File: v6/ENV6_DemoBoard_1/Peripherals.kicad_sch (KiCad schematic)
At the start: 21 parts, among them J301 Micro_SD_Card, J302 Conn_01x03_Pin, J303 Conn_02x02_Odd_Even, J304 Conn_02x02_Odd_Even, J305 Conn_02x02_Odd_Even, J306 Conn_02x02_Odd_Even, U301 PAC1954x-x4MX

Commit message: ENV6 (test): Changes after first review
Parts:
- removed J302: Conn_01x03_Pin, Connector_PinSocket_2.54mm:PinSocket_1x03_P2.54mm_Vertical, symbol Connector:Conn_01x03_Pin
- removed R303, R304: 10kR, Resistor_SMD:R_0603_1608Metric, symbol Device:R
- added J2: SHIELD_ARDUINO-UNO, connectors:arduino_uno_full, symbol connectors:Arduino Uno-Shield (Full)
- C301: value 100nF -> 100n
- C302: value 10uF -> 10µ
- C303: value 4.7uF -> 4µ7
- C304: value 0.1uF -> 100n
- R302: value 10kR -> 10k
- R305, R306: value 0R -> 0R1
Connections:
- net PAC_PWRDN: no longer names the net of R302.2, U301.16 (~{PWRDN})
- net PAC_SLOW: no longer names the net of R306.1, U301.1 (SLOW)
- new net: J2.G0 (GND), J2.G1 (GND), J2.G2 (GND)
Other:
- note added: "Add it to the MCU"
- note added: "Add these pins to the FPGA board"
- note added: "Sensing PAC #1 (MCU board) - 3V3 wireless - 3V3 only MCU - 3V3 MCU flash - 3v3 MCU peripherie (outside via connector)"
- note added: "Sensing PAC #2 (FPGA board) - FPGA core (1V8) - FPGA core (1V1) - FPGA peripherie (3V3) - FPGA IO-banks + flash (3V3)"
- note added: "Sensing PAC #3 (Power directly) - Input - Line output 1 - Line output 2 - Line output 3 - Line output 4 (?)"
- moved on the sheet: R302, R306

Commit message: new PSU and updates
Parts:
- removed J303, J304, J305, J306: Conn_02x02_Odd_Even, Connector_PinHeader_2.54mm:PinHeader_2x02_P2.54mm_Vertical, symbol Connector_Generic:Conn_02x02_Odd_Even
- added C14: 4µ7, Capacitor_SMD:C_0603_1608Metric, symbol Device:C
- added C15: 100n, Capacitor_SMD:C_0603_1608Metric, symbol Device:C
- added J401: Conn_02x12_Odd_Even, Connector_PinSocket_2.54mm:PinSocket_2x12_P2.54mm_Vertical, symbol Connector_Generic:Conn_02x12_Odd_Even
- added R5, R6: 0R1, Resistor_SMD:R_0603_1608Metric, symbol Device:R
- added R7: 10k, Resistor_SMD:R_0603_1608Metric, symbol Device:R
- added RS5, RS6, RS7, RS8: 0.82R, Resistor_SMD:R_0603_1608Metric, symbol Device:R
- added U2: PAC1954x-x4MX, Package_DFN_QFN:VQFN-16-1EP_3x3mm_P0.5mm_EP1.1x1.1mm, symbol Sensor_Energy:PAC1954x-x4MX
- J2: now not fitted; now left out of the parts list
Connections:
- net GND: now also C14.2, C15.2, R5.2, R6.2, U2.17 (EP), U2.3 (GND)
- net GP0/I2C0_SDA: now also U2.5 (SDA)
- net GP1/I2C0_SCL: now also U2.4 (SCL)
- net PSU_OUT1: now also RS5.2, U2.11 (SENSE1+); no longer RS1.2, U301.11 (SENSE1+)
- net PSU_OUT2: now also RS6.2, U2.13 (SENSE2+); no longer RS2.2, U301.13 (SENSE2+)
- net PSU_OUT3: now also RS7.2, U2.8 (SENSE3+); no longer RS3.2, U301.8 (SENSE3+)
- net PSU_OUT4: now also RS8.2, U2.10 (SENSE4+); no longer RS4.2, U301.10 (SENSE4+)
- net V1: now also J401.1 (Pin_1), J401.2 (Pin_2), J401.3 (Pin_3), J401.4 (Pin_4), RS5.1, U2.12 (SENSE1-); no longer RS1.1, U301.12 (SENSE1-)
- net V2: now also J401.10 (Pin_10), J401.7 (Pin_7), J401.8 (Pin_8), J401.9 (Pin_9), RS6.1, U2.14 (SENSE2-); no longer RS2.1, U301.14 (SENSE2-)
- net V3: now also J401.13 (Pin_13), J401.14 (Pin_14), J401.15 (Pin_15), J401.16 (Pin_16), RS7.1, U2.7 (SENSE3-); no longer RS3.1, U301.7 (SENSE3-)
- net V4: now also J401.19 (Pin_19), J401.20 (Pin_20), J401.21 (Pin_21), J401.22 (Pin_22), RS8.1, U2.9 (SENSE4-); no longer RS4.1, U301.9 (SENSE4-)
- net VCC_MCU: now also C14.1, C15.1, R7.1, U2.2 (V_{DD}); no longer C301.2, C302.2, J301.4 (VDD)
- net PAC_GPIO renamed PAC1_GPIO
- new net: R6.1, U2.1 (SLOW)
- new net: R7.2, U2.16 (~{PWRDN})
- new net: R5.1, U2.6 (ADDRSEL)
- new net 3V3_MCU: RS1.2, RS2.2, RS3.2, RS4.2, U301.10 (SENSE4+), U301.11 (SENSE1+), U301.13 (SENSE2+), U301.8 (SENSE3+)
- new net 3V3_MCU_FLASH: RS3.1, U301.7 (SENSE3-)
- new net 3V3_MCU_Per: C301.2, C302.2, J301.4 (VDD), RS4.1, U301.9 (SENSE4-)
- new net 3V3_MCU_only: RS1.1, U301.12 (SENSE1-)
- new net 3V3_Pi_Radio: RS2.1, U301.14 (SENSE2-)
- new net PAC2_GPIO: U2.15 (GPIO)
- no-connect marks 2 -> 10
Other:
- note added: "PAC1954 (1)"
- note added: "PAC1954 (2)"
- note added: "Sensing PAC #2 (Power directly) - Input - Line output 1 - Line output 2 - Line output 3 - Line output 4 (?)"
- note added: "Sensing PAC #3(FPGA board) - FPGA core (1V8) - FPGA core (1V1) - FPGA peripherie (3V3) - FPGA IO-banks + flash (3V3)"
- note removed: "PAC1954"
- note removed: "Sensing PAC #2 (FPGA board) - FPGA core (1V8) - FPGA core (1V1) - FPGA peripherie (3V3) - FPGA IO-banks + flash (3V3)"
- note removed: "Sensing PAC #3 (Power directly) - Input - Line output 1 - Line output 2 - Line output 3 - Line output 4 (?)"
- moved on the sheet: C301, C302, C303, C304, J301, R301, R302, R305, R306, RS1, RS2, RS3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

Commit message: Changes after second rev of ENV6 test
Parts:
- removed C14, C303: 4µ7, Capacitor_SMD:C_0603_1608Metric, symbol Device:C
- removed C15, C304: 100n, Capacitor_SMD:C_0603_1608Metric, symbol Device:C
- removed J2: SHIELD_ARDUINO-UNO, connectors:arduino_uno_full, symbol connectors:Arduino Uno-Shield (Full)
- removed J401: Conn_02x12_Odd_Even, Connector_PinSocket_2.54mm:PinSocket_2x12_P2.54mm_Vertical, symbol Connector_Generic:Conn_02x12_Odd_Even
- removed R301: 10kR, Resistor_SMD:R_0603_1608Metric, symbol Device:R
- removed R302, R7: 10k, Resistor_SMD:R_0603_1608Metric, symbol Device:R
- removed R305, R306, R5, R6: 0R1, Resistor_SMD:R_0603_1608Metric, symbol Device:R
- removed RS1, RS2, RS3, RS4, RS5, RS6, RS7, RS8: 0.82R, Resistor_SMD:R_0603_1608Metric, symbol Device:R
- removed U2, U301: PAC1954x-x4MX, Package_DFN_QFN:VQFN-16-1EP_3x3mm_P0.5mm_EP1.1x1.1mm, symbol Sensor_Energy:PAC1954x-x4MX
- added C26, C45, C49: 10u, Capacitor_SMD:C_0402_1005Metric, symbol passive:C0402
- added C27, C46, C50: 100n, Capacitor_SMD:C_0402_1005Metric, symbol passive:C0402
- added R14, R16, R21, R23, R24, R25, R29, R31, R32, R33, R36: 0R82, Resistor_SMD:R_0402_1005Metric, symbol passive:R0402
- added R15, R22, R28, R30: 10k, Resistor_SMD:R_0402_1005Metric, symbol passive:R0402
- added R17: 100k, Resistor_SMD:R_0402_1005Metric, symbol passive:R0402
- added R18, R27, R34, R35: 750R, Resistor_SMD:R_0402_1005Metric, symbol passive:R0402
- added R26: 0R1, Resistor_SMD:R_0402_1005Metric, symbol passive:R0402
- added U5, U7, U8: PAC1954x-x4MX, Package_DFN_QFN:VQFN-16-1EP_3x3mm_P0.5mm_EP1.1x1.1mm, symbol sensors:PAC1954x-x4MX
- C48: renamed from C302; value 10µ -> 10u
- renumbered C301 to C47, J301 to J2
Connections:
- net GND: now also C26.1, C27.1, C45.1, C46.1, C49.1, C50.1, R17.2, R18.2, R26.2, R27.2, R34.2, R35.2, U5.17 (EP), U5.3 (GND), U7.17 (EP), U7.3 (GND), U8.17 (EP), U8.3 (GND)
- net GP0/I2C0_SDA: now also U5.5 (SDA), U7.5 (SDA), U8.5 (SDA)
- net GP1/I2C0_SCL: now also U5.4 (SCL), U7.4 (SCL), U8.4 (SCL)
- net GP5/SPI0_CS: now also R28.1
- net PSU_OUT1: now also R29.2, U8.11 (SENSE1+)
- net PSU_OUT2: now also R31.2, U8.13 (SENSE2+)
- net PSU_OUT3: now also R32.2, U8.8 (SENSE3+)
- net PSU_OUT4: now also R33.2, U8.10 (SENSE4+)
- net V1: now also R29.1, U8.12 (SENSE1-)
- net V2: now also R31.1, U8.14 (SENSE2-)
- net V3: now also R32.1, U8.7 (SENSE3-)
- net V4: now also R33.1, U8.9 (SENSE4-)
- net 3V3_MCU_Per renamed VDDD_PERI
- net VDDD_PERI: now also C26.2, C27.2, C45.2, C46.2, C49.2, C50.2, R15.1, R22.1, R25.1, R28.2, R30.1, U5.2 (V_{DD}), U7.2 (V_{DD}), U7.9 (SENSE4-), U8.2 (V_{DD})
- new net: R18.1, U5.1 (SLOW)
- new net: R14.1, U5.12 (SENSE1-)
- new net: R15.2, U5.16 (~{PWRDN})
- new net: R17.1, U5.6 (ADDRSEL)
- new net: R30.2, U8.16 (~{PWRDN})
- new net: R34.1, U8.6 (ADDRSEL)
- new net: R22.2, U7.16 (~{PWRDN})
- new net: R26.1, U7.6 (ADDRSEL)
- new net: R35.1, U8.1 (SLOW)
- new net: R27.1, U7.1 (SLOW)
- new net VDDD_FLASH: R24.1, U7.7 (SENSE3-)
- new net VDDD_MCU: R21.1, U7.12 (SENSE1-)
- new net VDDD_RADIO: R23.1, U7.14 (SENSE2-)
- new net VDIG_IN: R16.1, U5.14 (SENSE2-)
- new net VDIG_OUT: R21.2, R23.2, R24.2, R25.2, U7.10 (SENSE4+), U7.11 (SENSE1+), U7.13 (SENSE2+), U7.8 (SENSE3+)
- new net VPERI_IN: R36.1, U5.7 (SENSE3-)
- new net VSYS_IN: R14.2, R16.2, R36.2, U5.11 (SENSE1+), U5.13 (SENSE2+), U5.8 (SENSE3+)
- no-connect marks 10 -> 7
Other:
- note added: "1, Peripherals"
- note added: "I2C Addr: 0x10"
- note added: "I2C Addr: 0x12"
- note added: "I2C Addr: 0x1C"
- note added: "PAC1954 (3)"
- note added: "Sensing PAC #1 - 3V3 wireless - 3V3 only MCU - 3V3 MCU flash - 3v3 peri"
- note added: "Sensing PAC #2 - Line output 1 - Line output 2 - Line output 3 - Line output 4"
- note added: "Sensing PAC #3(FPGA board) - FPGA core (1V8) - FPGA core (1V1) - FPGA peripherie (3V3) - FPGA IO-banks + flash (3V3) Acutally it is doubled, maybe remove it?"
- note added: "Sensing PAC #4 - V_SYS Input - V_DIG - V_APP - ???"
- note added: "find a link to buy sense resistors (0.1% accuracy, high power budget)"
- note removed: "3, Peripherals"
- note removed: "Add it to the MCU"
- note removed: "Add these pins to the FPGA board"
- note removed: "Sensing PAC #1 (MCU board) - 3V3 wireless - 3V3 only MCU - 3V3 MCU flash - 3v3 MCU peripherie (outside via connector)"
- note removed: "Sensing PAC #2 (Power directly) - Input - Line output 1 - Line output 2 - Line output 3 - Line output 4 (?)"
- note removed: "Sensing PAC #3(FPGA board) - FPGA core (1V8) - FPGA core (1V1) - FPGA peripherie (3V3) - FPGA IO-banks + flash (3V3)"
- note removed: "Voltage Outputs"
- moved on the sheet: C47, C48, J2

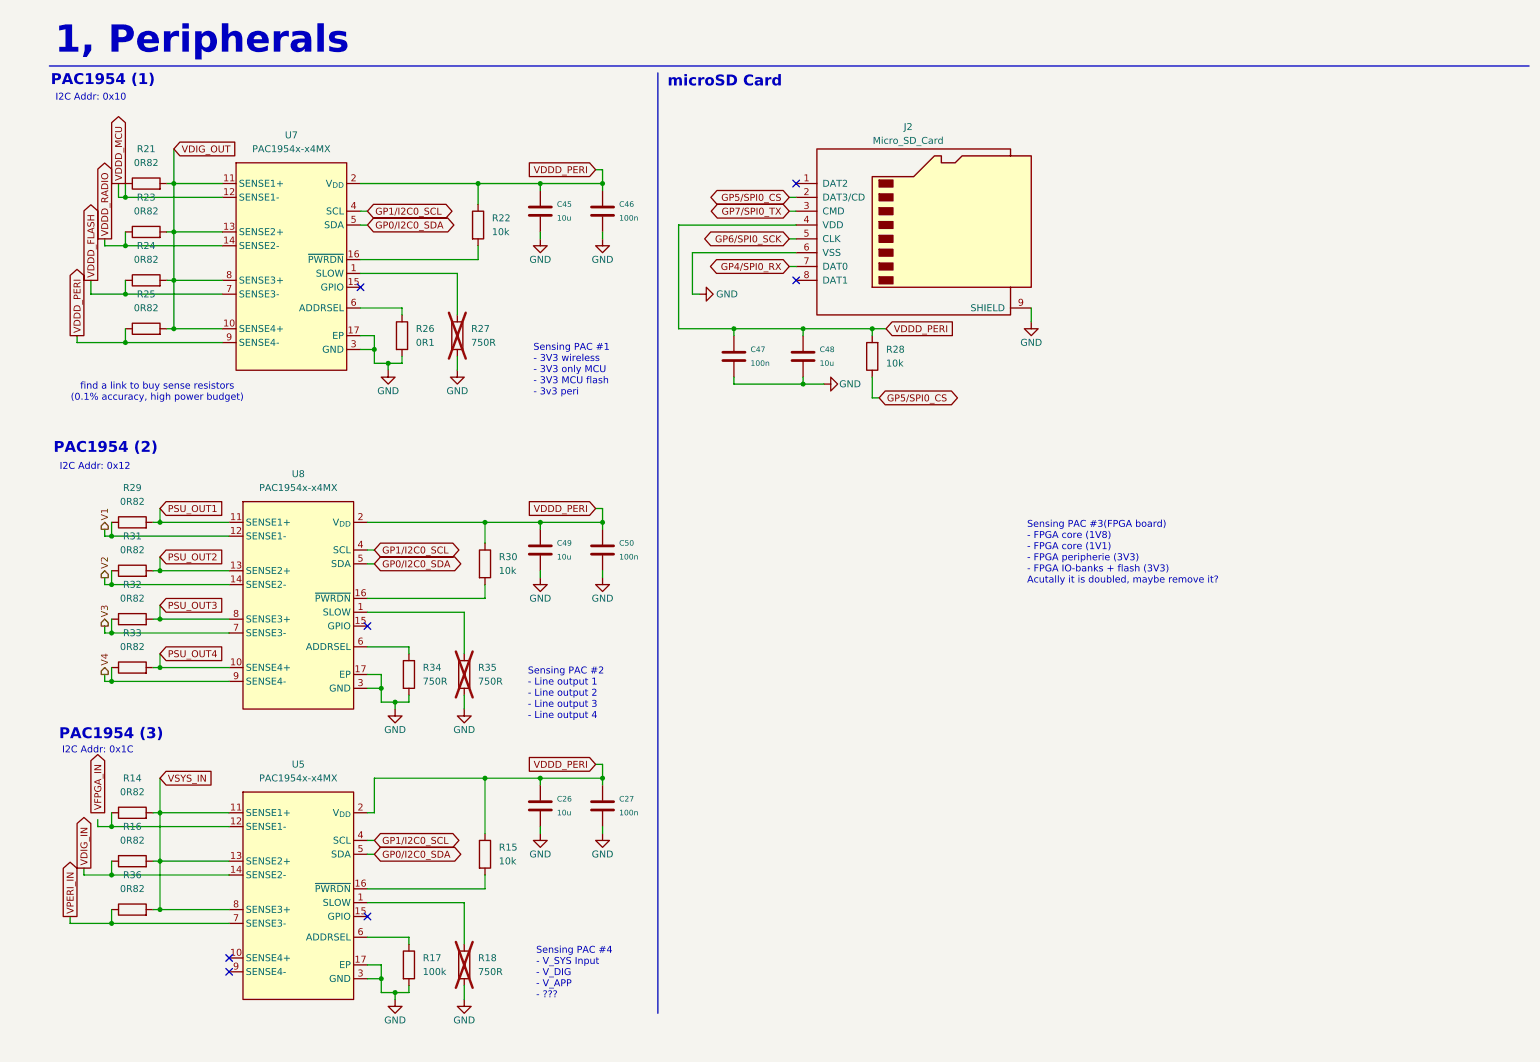
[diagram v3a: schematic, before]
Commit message: update Demoboard and add GateMateA11 board
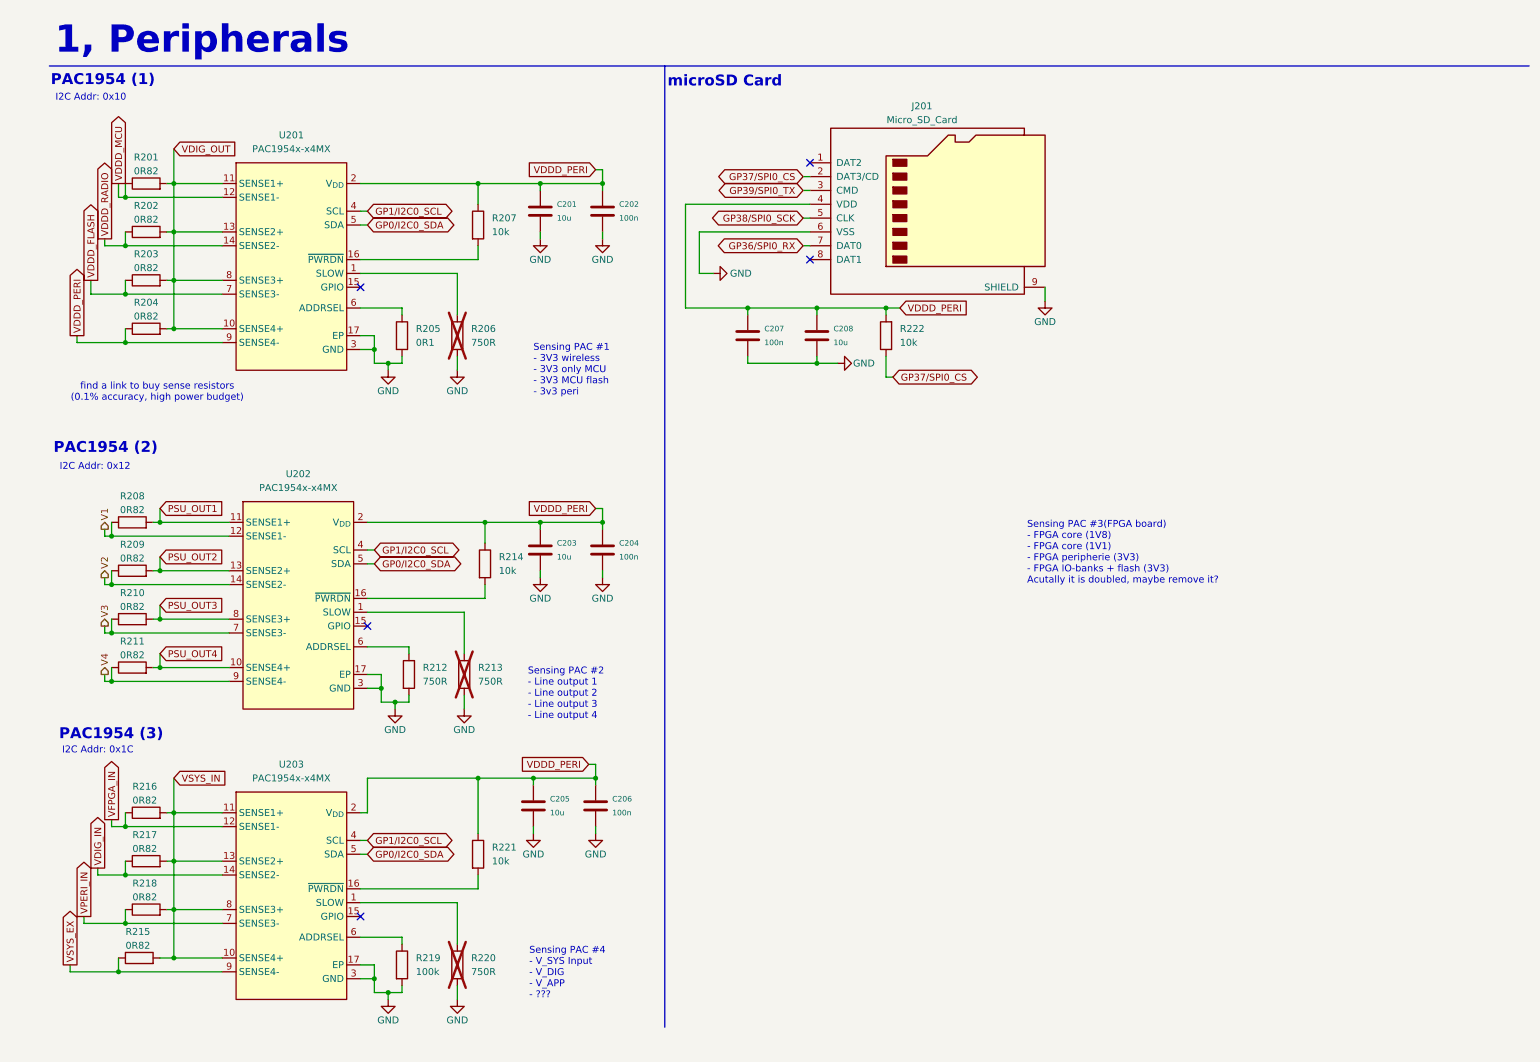
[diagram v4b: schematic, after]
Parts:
- added R215: 0R82, Resistor_SMD:R_0603_1608Metric, symbol passive:R0402
- R201: renamed from R21; footprint Resistor_SMD:R_0402_1005Metric -> Resistor_SMD:R_0603_1608Metric
- R202: renamed from R23; footprint Resistor_SMD:R_0402_1005Metric -> Resistor_SMD:R_0603_1608Metric
- R203: renamed from R24; footprint Resistor_SMD:R_0402_1005Metric -> Resistor_SMD:R_0603_1608Metric
- R204: renamed from R25; footprint Resistor_SMD:R_0402_1005Metric -> Resistor_SMD:R_0603_1608Metric
- R208: renamed from R29; footprint Resistor_SMD:R_0402_1005Metric -> Resistor_SMD:R_0603_1608Metric
- R209: renamed from R31; footprint Resistor_SMD:R_0402_1005Metric -> Resistor_SMD:R_0603_1608Metric
- R210: renamed from R32; footprint Resistor_SMD:R_0402_1005Metric -> Resistor_SMD:R_0603_1608Metric
- R211: renamed from R33; footprint Resistor_SMD:R_0402_1005Metric -> Resistor_SMD:R_0603_1608Metric
- R216: renamed from R14; footprint Resistor_SMD:R_0402_1005Metric -> Resistor_SMD:R_0603_1608Metric
- R217: renamed from R16; footprint Resistor_SMD:R_0402_1005Metric -> Resistor_SMD:R_0603_1608Metric
- R218: renamed from R36; footprint Resistor_SMD:R_0402_1005Metric -> Resistor_SMD:R_0603_1608Metric
- renumbered C45 to C201, C46 to C202, C49 to C203, C50 to C204, C26 to C205, C27 to C206, C47 to C207, C48 to C208, J2 to J201, R26 to R205, R27 to R206, R22 to R207, R34 to R212, R35 to R213, R30 to R214, R17 to R219, R18 to R220, R15 to R221, R28 to R222, U7 to U201, U8 to U202, U5 to U203
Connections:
- net VFPGA_IN: now also R216.1, U203.12 (SENSE1-)
- net VSYS_IN: now also U203.10 (SENSE4+), R215.2
- net VSYS_EX: now reaches U203.9 (SENSE4-)
- net VSYS_EX: now also R215.1
- net GP4/SPI0_RX renamed GP36/SPI0_RX
- net GP5/SPI0_CS renamed GP37/SPI0_CS
- net GP6/SPI0_SCK renamed GP38/SPI0_SCK
- net GP7/SPI0_TX renamed GP39/SPI0_TX
- no-connect marks 7 -> 5
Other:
- moved on the sheet: C205, C206, C207, C208, J201, R216, R217, R218, R219, R220, R221, R222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
